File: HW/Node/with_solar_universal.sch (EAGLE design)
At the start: 16 parts, among them U1 MS560702BA03-50, U2 HDC2080DMBR, U3 RFM69HW, X1 734120110

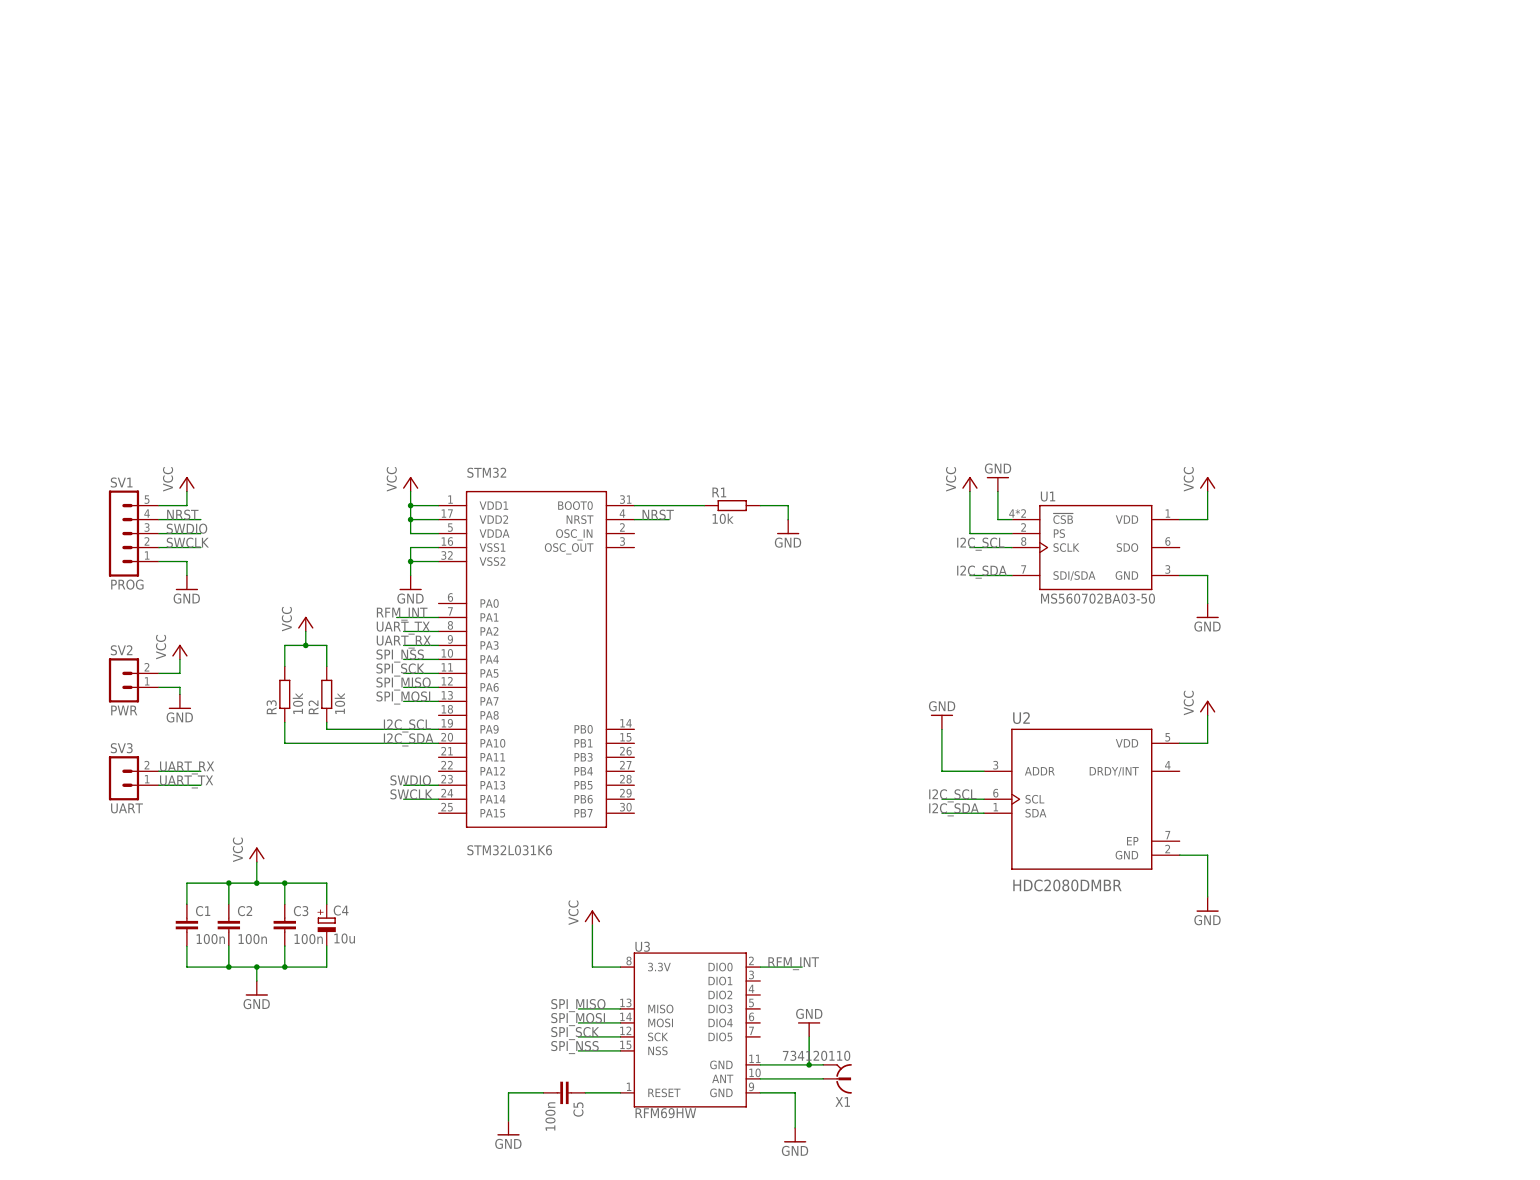
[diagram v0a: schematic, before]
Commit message: HW: Update node schematic and board
Signed-off-by: Ales Musil <aedvin1@gmail.com>
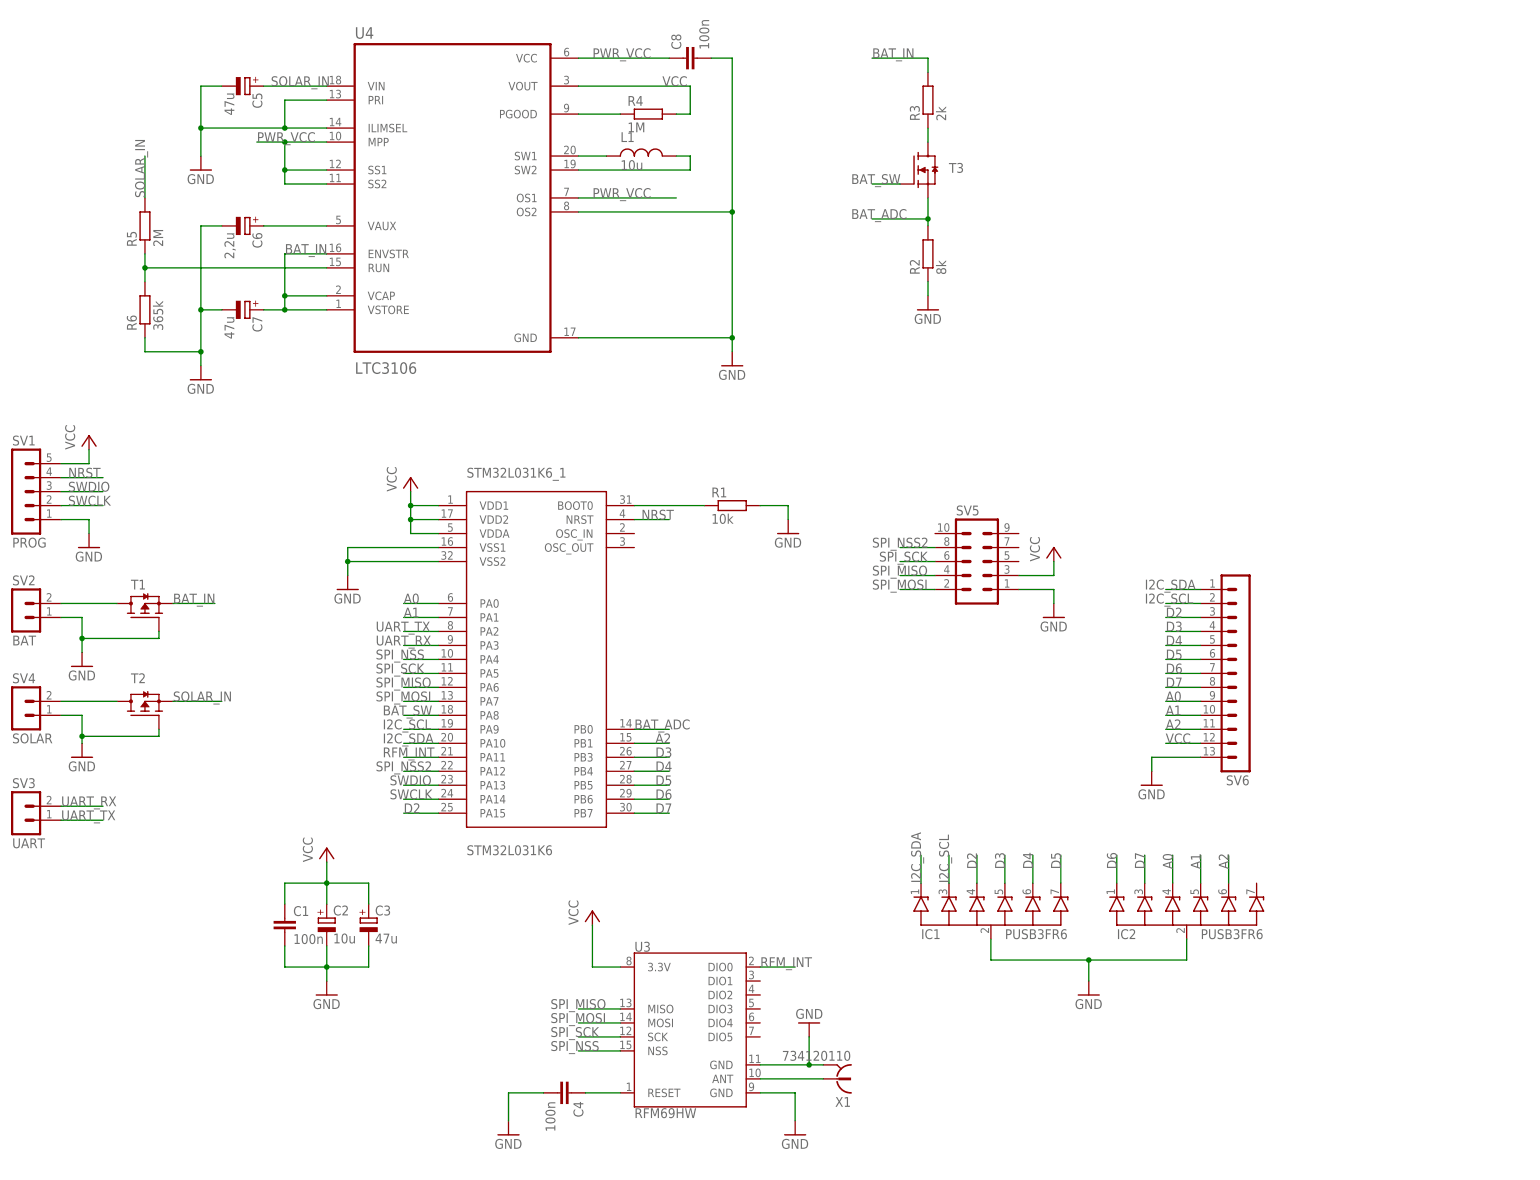
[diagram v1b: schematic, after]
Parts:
- removed U1: MS560702BA03-50, MS560702BA03-50:MS560702BA03-50
- removed U2: HDC2080DMBR, HDC2080DMBR2:HDC2080DMBR
- added C6: 2,2u, rcl:CPOL-EUUD-4X5,8
- added C7: 47u, rcl:CPOL-EUUD-4X5,8
- added C8: 100n, rcl:C-EUC1206
- added IC1, IC2: PUSB3FR6, esd:PUSB3FR6
- added L1: 10u, dp:L1210
- added R4: 1M, rcl:R-EU_R0805
- added R5: 2M, rcl:R-EU_R0805
- added R6: 365k, rcl:R-EU_R0805
- added SV4: SOLAR, dp:MA02-1
- added SV5: (no value), con-lstb:MA05-2
- added SV6: (no value), con-lstb:MA13-1
- added T1, T2: RTQ035P02HZG, dp:RTQ035P02HZG
- added T3: RQ6E050AJTCR, dp:RQ6E050AJTCR
- added U4: LTC3106, LTC3106:LTC3106
- C2: value 100n -> 10u; device rcl:C-EUC1206 -> rcl:CPOL-EUUD-4X5,8
- C3, C5: value 100n -> 47u; device rcl:C-EUC1206 -> rcl:CPOL-EUUD-4X5,8
- C4: value 10u -> 100n; device rcl:CPOL-EUUD-4X5,8 -> rcl:C-EUC1206
- R2: value 10k -> 8k
- R3: value 10k -> 2k
- SV2: value PWR -> BAT
- renumbered STM32 to STM32L031K6_1
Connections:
- new net A0: IC2.4, STM32L031K6_1.PA0, SV6.9
- new net A1: IC2.5, STM32L031K6_1.PA1, SV6.10
- new net A2: IC2.6, STM32L031K6_1.PB1, SV6.11
- new net BAT_ADC: R2.2, STM32L031K6_1.PB0, T3.S
- new net BAT_IN: C7.+, R3.2, T1.S, U4.ENVSTR, U4.VCAP, U4.VSTORE
- new net BAT_SW: STM32L031K6_1.PA8, T3.G
- new net D2: IC1.4, STM32L031K6_1.PA15, SV6.3
- new net D3: IC1.5, STM32L031K6_1.PB3, SV6.4
- new net D4: IC1.6, STM32L031K6_1.PB4, SV6.5
- new net D5: IC1.7, STM32L031K6_1.PB5, SV6.6
- new net D6: IC2.1, STM32L031K6_1.PB6, SV6.7
- new net D7: IC2.3, STM32L031K6_1.PB7, SV6.8
- new net N$19: R3.1, T3.D
- new net N$3: L1.1, U4.SW1
- new net N$4: L1.2, U4.SW2
- new net N$5: C6.+, U4.VAUX
- new net N$6: R4.1, U4.PGOOD
- new net N$7: R5.1, R6.2, U4.RUN
- new net PWR_VCC: C8.1, U4.MPP, U4.OS1, U4.SS1, U4.SS2, U4.VCC
- new net SOLAR_IN: C5.+, R5.2, T2.S, U4.VIN
- new net SPI_NSS2: STM32L031K6_1.PA12, SV5.8
- new net T1: SV2.3, T1.D
- new net T2: SV4.3, T2.D
- net GND: now also C2.-, C3.-, C4.2, C5.-, C6.-, C7.-, C8.2, IC1.2, IC2.2, R2.1, R6.1, SV4.2, SV5.1, SV6.13, T1.G, T2.G, U4.GND, U4.ILIMSEL, U4.OS2, U4.PRI; no longer C2.2, C3.2, C4.-, C5.2, U1.!CSB, U1.GND, U2.ADDR, U2.GND
- net I2C_SCL: now also IC1.3, SV6.2; no longer R2.1, U1.SCLK, U2.SCL
- net I2C_SDA: now also IC1.1, SV6.1; no longer R3.1, U1.SDI/SDA, U2.SDA
- net N$10: now also C4.1; no longer C5.1
- net RFM_INT: now also STM32L031K6_1.PA11; no longer STM32L031K6_1.PA1
- net SPI_MISO: now also SV5.4
- net SPI_MOSI: now also SV5.2
- net SPI_SCK: now also SV5.6
- net VCC: now also C2.+, C3.+, R4.2, SV5.3, SV6.12, U4.VOUT; no longer C2.1, C3.1, C4.+, R2.2, R3.2, SV2.3, U1.PS, U1.VDD, U2.VDD
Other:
- moved on the sheet: C1, R2, R3, SV1, SV2, SV3

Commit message: HW: Update node schematic and board
- Use different input protection.
- Add current limiting resistor.
- Add AAA battery holder.

Signed-off-by: Ales Musil <aedvin1@gmail.com>
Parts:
- removed IC1, IC2: PUSB3FR6, esd:PUSB3FR6
- removed SV1: PROG, con-lstb:MA05-1
- removed SV2: BAT, dp:MA02-1
- removed SV3: UART, dp:MA02-1
- removed SV4: SOLAR, dp:MA02-1
- removed SV5: (no value), con-lstb:MA05-2
- removed SV6: (no value), con-lstb:MA13-1
- added D1, D10, D11, D2, D3, D4, D5, D6, D7, D8, D9: BAS70-04, nxp_60:BAS70-04
- added J1: 1076, 1076:1076
- added R10, R11, R12, R13, R14, R7, R8, R9: 300R, rcl:R-EU_R0805
- added U$1, U$2, U$3: SJ-C, dp:SJ-C
- added U$4, U$5, U$6: MA02-1, dp:MA02-1
- added U$7: MA05-1, dp:MA05-1
- added U$8: MA05-2, dp:MA05-2
- added U$9: MA13-1, dp:MA13-1
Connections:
- new net N$11: R9.1, U$9.3
- new net N$12: R10.1, U$9.4
- new net N$13: R11.1, U$9.5
- new net N$14: R12.1, U$9.6
- new net N$15: R13.1, U$9.7
- new net N$16: R14.1, U$9.8
- new net N$17: U$1.2, U$9.9
- new net N$18: U$2.2, U$9.10
- new net N$20: U$3.2, U$9.11
- new net N$8: R7.1, U$9.1
- new net N$9: R8.1, U$9.2
- net A0: now also D9.K1A2, U$1.1; no longer IC2.4, SV6.9
- net A1: now also D10.K1A2, U$2.1; no longer IC2.5, SV6.10
- net A2: now also D11.K1A2, U$3.1; no longer IC2.6, SV6.11
- net BAT_IN: now also U$8.3
- net D2: now also D3.K1A2, R9.2; no longer IC1.4, SV6.3
- net D3: now also D4.K1A2, R10.2; no longer IC1.5, SV6.4
- net D4: now also D5.K1A2, R11.2; no longer IC1.6, SV6.5
- net D5: now also D6.K1A2, R12.2; no longer IC1.7, SV6.6
- net D6: now also D7.K1A2, R13.2; no longer IC2.1, SV6.7
- net D7: now also D8.K1A2, R14.2; no longer IC2.3, SV6.8
- net GND: now also D1.A1, D10.A1, D11.A1, D2.A1, D3.A1, D4.A1, D5.A1, D6.A1, D7.A1, D8.A1, D9.A1, J1.-, U$4.2, U$5.2, U$7.1, U$8.1, U$9.13; no longer IC1.2, IC2.2, SV1.1, SV2.2, SV4.2, SV5.1, SV6.13
- net I2C_SCL: now also D2.K1A2, R8.2; no longer IC1.3, SV6.2
- net I2C_SDA: now also D1.K1A2, R7.2; no longer IC1.1, SV6.1
- net NRST: now also U$7.4; no longer SV1.4
- net SPI_MISO: now also U$8.4; no longer SV5.4
- net SPI_MOSI: now also U$8.2; no longer SV5.2
- net SPI_NSS2: now also U$8.8; no longer SV5.8
- net SPI_SCK: now also U$8.6; no longer SV5.6
- net SWCLK: now also U$7.2; no longer SV1.2
- net SWDIO: now also U$7.3; no longer SV1.3
- net T1: now also J1.+, U$4.3; no longer SV2.3
- net T2: now also U$5.3; no longer SV4.3
- net UART_RX: now also U$6.3; no longer SV3.3
- net UART_TX: now also U$6.2; no longer SV3.2
- net VCC: now also D1.K2, D10.K2, D11.K2, D2.K2, D3.K2, D4.K2, D5.K2, D6.K2, D7.K2, D8.K2, D9.K2, U$7.5, U$9.12; no longer SV1.5, SV5.3, SV6.12
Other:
- moved on the sheet: T1, T2
